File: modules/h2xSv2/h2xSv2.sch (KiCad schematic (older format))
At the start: 14 parts, among them J1 Conn_01x10_Male, J10 Conn_01x02_Male, J2 Conn_01x10_Male, J3 Conn_01x10_Male, J4 Conn_01x10_Male, J5 Conn_01x04_Male, J6 Conn_01x04_Male, J7 Conn_01x12_Male, J8 Conn_01x12_Male, J9 Conn_01x12_Male

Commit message: Fix holes and edges
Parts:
- added H5, H6, H7, H8: MountingHole, MountingHole:MountingHole_3.2mm_M3, symbol Mechanical:MountingHole
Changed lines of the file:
@@
+	1    0    0    -1
+$EndComp
+$Comp
+L Mechanical:MountingHole H5
+U 1 1 5E7BCAAE
+P 8750 2500
+F 0 "H5" H 8850 2546 50  0000 L CNN
+F 1 "MountingHole" H 8850 2455 50  0000 L CNN
+F 2 "MountingHole:MountingHole_3.2mm_M3" H 8750 2500 50  0001 C CNN
+F 3 "~" H 8750 2500 50  0001 C CNN
+	1    8750 2500
+	1    0    0    -1
+$EndComp
+$Comp
+L Mechanical:MountingHole H6
+U 1 1 5E7BCF2B
+P 8750 3000
+F 0 "H6" H 8850 3046 50  0000 L CNN
+F 1 "MountingHole" H 8850 2955 50  0000 L CNN
+F 2 "MountingHole:MountingHole_3.2mm_M3" H 8750 3000 50  0001 C CNN
+F 3 "~" H 8750 3000 50  0001 C CNN
+	1    8750 3000
+	1    0    0    -1
+$EndComp
+$Comp
+L Mechanical:MountingHole H7
+U 1 1 5E7BD33B
+P 8750 3500
+F 0 "H7" H 8850 3546 50  0000 L CNN
+F 1 "MountingHole" H 8850 3455 50  0000 L CNN
+F 2 "MountingHole:MountingHole_3.2mm_M3" H 8750 3500 50  0001 C CNN
+F 3 "~" H 8750 3500 50  0001 C CNN
+	1    8750 3500
+	1    0    0    -1
+$EndComp
+$Comp
+L Mechanical:MountingHole H8
+U 1 1 5E7BD737
+P 8750 4000
+F 0 "H8" H 8850 4046 50  0000 L CNN
+F 1 "MountingHole" H 8850 3955 50  0000 L CNN
+F 2 "MountingHole:MountingHole_3.2mm_M3" H 8750 4000 50  0001 C CNN
+F 3 "~" H 8750 4000 50  0001 C CNN
+	1    8750 4000
 	1    0    0    -1
 $EndComp

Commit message: h2xS v2 in work
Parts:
- added J11: Conn_01x06_Male, Connector_PinHeader_2.54mm:PinHeader_1x06_P2.54mm_Vertical, symbol Connector:Conn_01x06_Male
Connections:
- net A0: now also J11.6 (Pin_6)
- net A1: now also J11.5 (Pin_5)
- net A2: now also J11.4 (Pin_4)
- net A3: now also J11.3 (Pin_3)
- net A4: now also J11.2 (Pin_2)
- net A5: now also J11.1 (Pin_1)
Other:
- moved on the sheet: J3
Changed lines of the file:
@@
 L Connector:Conn_01x10_Male J3
 U 1 1 5E7C4275
-P 2450 2400
-F 0 "J3" H 2500 2900 50  0000 R CNN
-F 1 "Conn_01x10_Male" V 2350 2650 50  0000 R CNN
-F 2 "Connector_PinSocket_2.54mm:PinSocket_1x10_P2.54mm_Vertical" H 2450 2400 50  0001 C CNN
-F 3 "~" H 2450 2400 50  0001 C CNN
-	1    2450 2400
+P 3200 2400
+F 0 "J3" H 3250 2900 50  0000 R CNN
+F 1 "Conn_01x10_Male" V 3100 2650 50  0000 R CNN
+F 2 "Connector_PinSocket_2.54mm:PinSocket_1x10_P2.54mm_Vertical" H 3200 2400 50  0001 C CNN
+F 3 "~" H 3200 2400 50  0001 C CNN
+	1    3200 2400
 	-1   0    0    -1
 $EndComp
@@
 Text Label 2000 3600 0    50   ~ 0
 SDA
-Wire Wire Line
-	1750 2000 2250 2000
 Connection ~ 1750 2000
 Wire Wire Line
@@
 	1750 2200 2075 2200
 Wire Wire Line
-	1750 2300 2250 2300
-Wire Wire Line
-	1750 2400 2250 2400
-Wire Wire Line
-	1750 2500 2250 2500
-Wire Wire Line
-	1750 2600 2250 2600
-Wire Wire Line
 	1750 2700 2225 2700
 Wire Wire Line
 	1750 2800 2150 2800
-Wire Wire Line
-	1750 2900 2250 2900
 Connection ~ 1750 2900
 Wire Wire Line
@@
 Connection ~ 2175 2100
 Wire Wire Line
-	2175 2100 2250 2100
-Wire Wire Line
 	5550 3125 5550 3050
 Wire Wire Line
@@
 	6625 3125 5650 3125
 Connection ~ 2075 2200
-Wire Wire Line
-	2075 2200 2250 2200
 $Comp
 L power:GND #PWR01004
@@
 Connection ~ 2150 2800
 Wire Wire Line
-	2150 2800 2250 2800
-Wire Wire Line
 	2225 2700 2225 3325
 Wire Wire Line
@@
 	2375 3325 2375 3600
 Connection ~ 2225 2700
-Wire Wire Line
-	2225 2700 2250 2700
 Connection ~ 2375 3600
 Wire Wire Line
@@
 	1    0    0    -1
 $EndComp
+Wire Wire Line
+	1750 2000 3000 2000
+Wire Wire Line
+	2175 2100 3000 2100
+Wire Wire Line
+	2075 2200 3000 2200
+Wire Wire Line
+	1750 2300 2850 2300
+Wire Wire Line
+	1750 2400 2750 2400
+Wire Wire Line
+	1750 2500 2650 2500
+Wire Wire Line
+	1750 2600 2550 2600
+Wire Wire Line
+	2225 2700 2450 2700
+Wire Wire Line
+	2150 2800 2350 2800
+Wire Wire Line
+	1750 2900 3000 2900
+$Comp
+L Connector:Conn_01x06_Male J11
+U 1 1 5E7DADE2
+P 2550 3200
+F 0 "J11" V 2704 2812 50  0000 R CNN
+F 1 "Conn_01x06_Male" V 2450 3275 50  0000 R CNN
+F 2 "Connector_PinHeader_2.54mm:PinHeader_1x06_P2.54mm_Vertical" H 2550 3200 50  0001 C CNN
+F 3 "~" H 2550 3200 50  0001 C CNN
+	1    2550 3200
+	0    -1   -1   0
+$EndComp
+Wire Wire Line
+	2350 3000 2350 2800
+Connection ~ 2350 2800
+Wire Wire Line
+	2350 2800 3000 2800
+Wire Wire Line
+	2450 3000 2450 2700
+Connection ~ 2450 2700
+Wire Wire Line
+	2450 2700 3000 2700
+Wire Wire Line
+	2550 3000 2550 2600
+Connection ~ 2550 2600
+Wire Wire Line
+	2550 2600 3000 2600
+Wire Wire Line
+	2650 3000 2650 2500
+Connection ~ 2650 2500
+Wire Wire Line
+	2650 2500 3000 2500
+Wire Wire Line
+	2750 3000 2750 2400
+Connection ~ 2750 2400
+Wire Wire Line
+	2750 2400 3000 2400
+Wire Wire Line
+	2850 3000 2850 2300
+Connection ~ 2850 2300
+Wire Wire Line
+	2850 2300 3000 2300
 $EndSCHEMATC

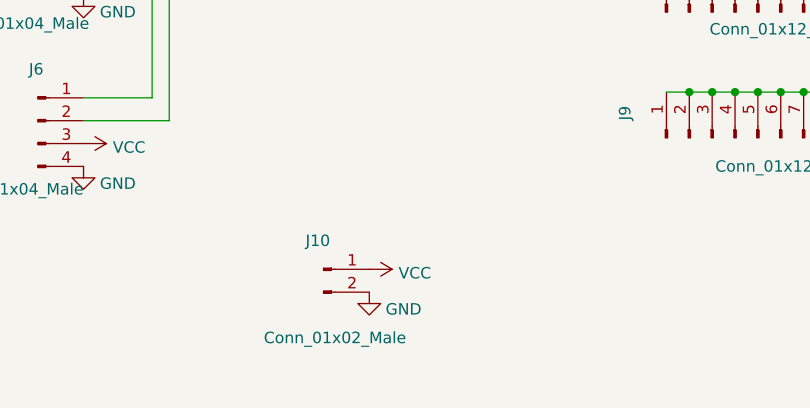
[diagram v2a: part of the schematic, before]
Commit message: h2xS - Reverse polarity protection was added
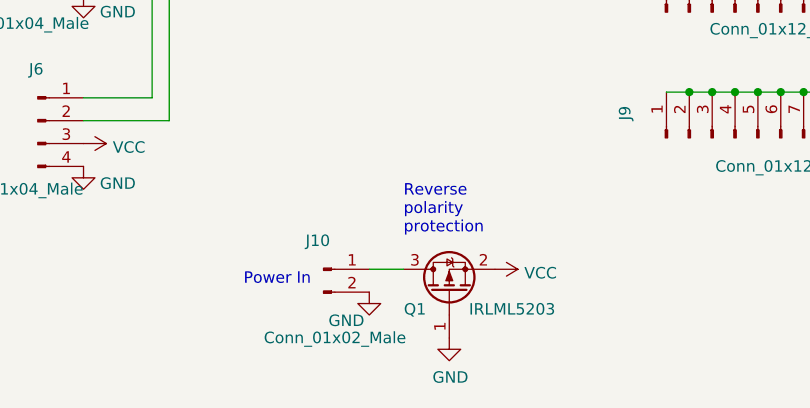
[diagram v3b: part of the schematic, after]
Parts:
- added Q1: IRLML5203, Package_TO_SOT_SMD:SOT-23, symbol Transistor_FET:IRLML5203
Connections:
- net GND: now also Q1.1 (G)
- net VCC: now also Q1.2 (S); no longer J10.1 (Pin_1)
- new net: J10.1 (Pin_1), Q1.3 (D)
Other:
- note added: "Power In"
- note added: "Reverse\npolarity\nprotection"
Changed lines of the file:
@@
 EESchema Schematic File Version 4
-LIBS:h2xSv2-cache
 EELAYER 30 0
 EELAYER END
@@
 L power:VCC #PWR01007
 U 1 1 5E83DD85
-P 3250 5000
-F 0 "#PWR01007" H 3250 4850 50  0001 C CNN
-F 1 "VCC" V 3267 5128 50  0000 L CNN
-F 2 "" H 3250 5000 50  0001 C CNN
-F 3 "" H 3250 5000 50  0001 C CNN
-	1    3250 5000
+P 3800 5000
+F 0 "#PWR01007" H 3800 4850 50  0001 C CNN
+F 1 "VCC" V 3817 5128 50  0000 L CNN
+F 2 "" H 3800 5000 50  0001 C CNN
+F 3 "" H 3800 5000 50  0001 C CNN
+	1    3800 5000
 	0    1    1    0
 $EndComp
@@
 P 3250 5100
 F 0 "#PWR01008" H 3250 4850 50  0001 C CNN
-F 1 "GND" H 3400 5025 50  0000 C CNN
+F 1 "GND" H 3150 4975 50  0000 C CNN
 F 2 "" H 3250 5100 50  0001 C CNN
 F 3 "" H 3250 5100 50  0001 C CNN
@@
 Wire Wire Line
 	2850 2300 3000 2300
+$Comp
+L Transistor_FET:IRLML5203 Q1
+U 1 1 60EE88DC
+P 3600 5100
+F 0 "Q1" V 3525 5250 50  0000 C CNN
+F 1 "IRLML5203" V 3525 4825 50  0000 C CNN
+F 2 "Package_TO_SOT_SMD:SOT-23" H 3800 5025 50  0001 L CIN
+F 3 "https://www.infineon.com/dgdl/irlml5203pbf.pdf?fileId=5546d462533600a40153566868da261d" H 3600 5100 50  0001 L CNN
+	1    3600 5100
+	0    -1   -1   0
+$EndComp
+Wire Wire Line
+	3250 5000 3400 5000
+$Comp
+L power:GND #PWR01
+U 1 1 60F02104
+P 3600 5300
+F 0 "#PWR01" H 3600 5050 50  0001 C CNN
+F 1 "GND" H 3605 5127 50  0000 C CNN
+F 2 "" H 3600 5300 50  0001 C CNN
+F 3 "" H 3600 5300 50  0001 C CNN
+	1    3600 5300
+	1    0    0    -1
+$EndComp
+Text Notes 2700 5075 0    50   ~ 0
+Power In
+Text Notes 3400 4850 0    50   ~ 0
+Reverse\npolarity\nprotection
 $EndSCHEMATC
